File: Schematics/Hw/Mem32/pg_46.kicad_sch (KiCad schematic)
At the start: 3 parts, among them U4701 F00, U4702 F00, U4703 F00

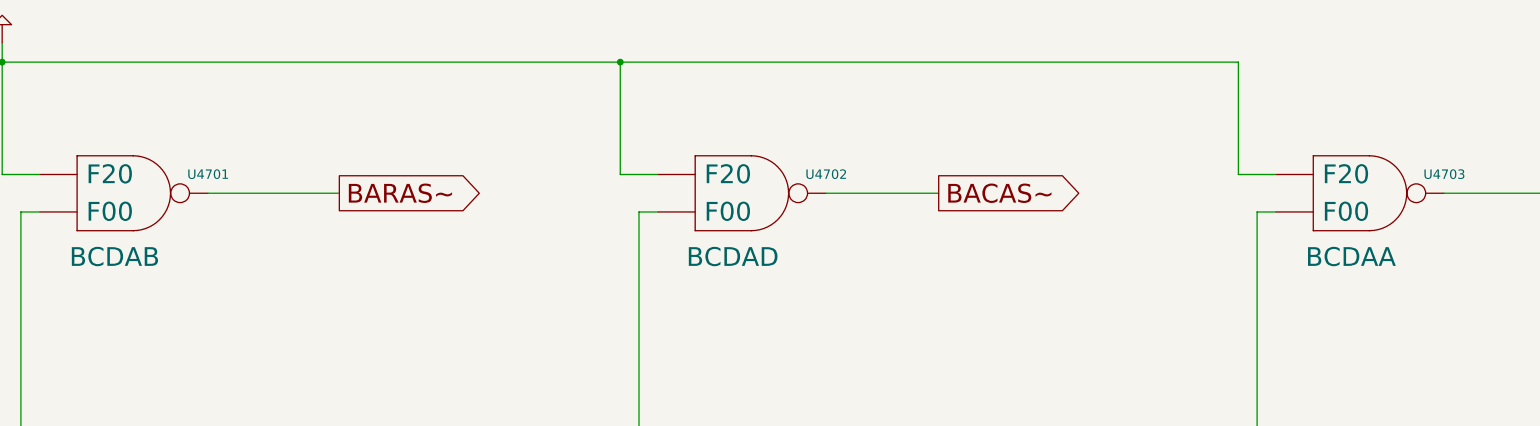
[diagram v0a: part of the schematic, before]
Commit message: Upgrade to KiCad9
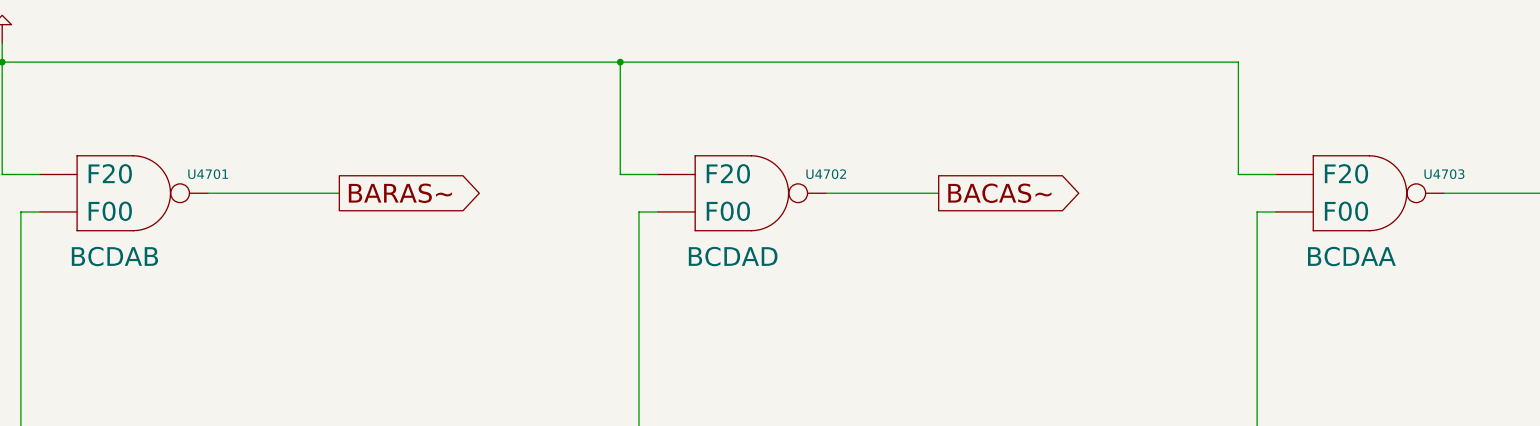
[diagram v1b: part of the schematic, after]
